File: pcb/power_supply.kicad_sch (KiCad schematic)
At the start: 34 parts

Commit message: Further schematic capture
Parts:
- removed C? (x2): 100u, symbol Device:C_Polarized
- removed C?: 10u, symbol Device:C
- removed U?: AMS1117-3.3, Package_TO_SOT_SMD:SOT-223-3_TabPin2, symbol Regulator_Linear:AMS1117-3.3
- added C?: 100n, symbol Device:C
- added J?: TO_IO, symbol adatv2:Connector_IO
- added U?: 74HC14, symbol 74xx:74HC14
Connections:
- net +3.3V: now also C?.1, J?.5 (3V3), J?.6 (3V3), U?.14 (VCC)
- net +5V: now also J?.3 (5V), J?.4 (5V)
- net GND: now also C?.2, U?.7 (GND)
- new net +12V: J?.1 (12V), J?.2 (12V)
- new net ADAT_IN1: J?.9 (ADAT_IN1)
- new net ADAT_IN2: J?.11 (ADAT_IN2)
- new net ADAT_OUT1: J?.13 (ADAT_OUT1)
- new net ADAT_OUT2: J?.15 (ADAT_OUT2)
- new net ADAT_THRU1: J?.17 (ADAT_THRU1)
- new net ADAT_THRU2: J?.19 (ADAT_THRU2)
- new net GND_IO: J?.10 (GND), J?.12 (GND), J?.14 (GND), J?.16 (GND), J?.18 (GND), J?.20 (GND), J?.7 (GND), J?.8 (GND)
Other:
- moved on the sheet: C?, L?, U?A

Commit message: Further schematic capture
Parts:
- added C? (x4): 100n, symbol Device:C
- added U? (x4): 74LVC2G17, symbol 74xGxx:74LVC2G17
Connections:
- net +3.3V: now also C?.1, C?.1, C?.1, C?.1, U?.5 (VCC), U?.5 (VCC), U?.5 (VCC), U?.5 (VCC)
- net GND: now also C?.2, C?.2, C?.2, C?.2, U?.2 (GND), U?.2 (GND), U?.2 (GND), U?.2 (GND)
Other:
- note added: "FPGA decoupling capacitors"
- note added: "IC supplies"
- note added: "IDC Connector"
- note added: "MCU decoupling capacitors"
- note removed: "FPGA decoupling caps"
- note removed: "MCU decoupling caps"
- moved on the sheet: C?, U?G

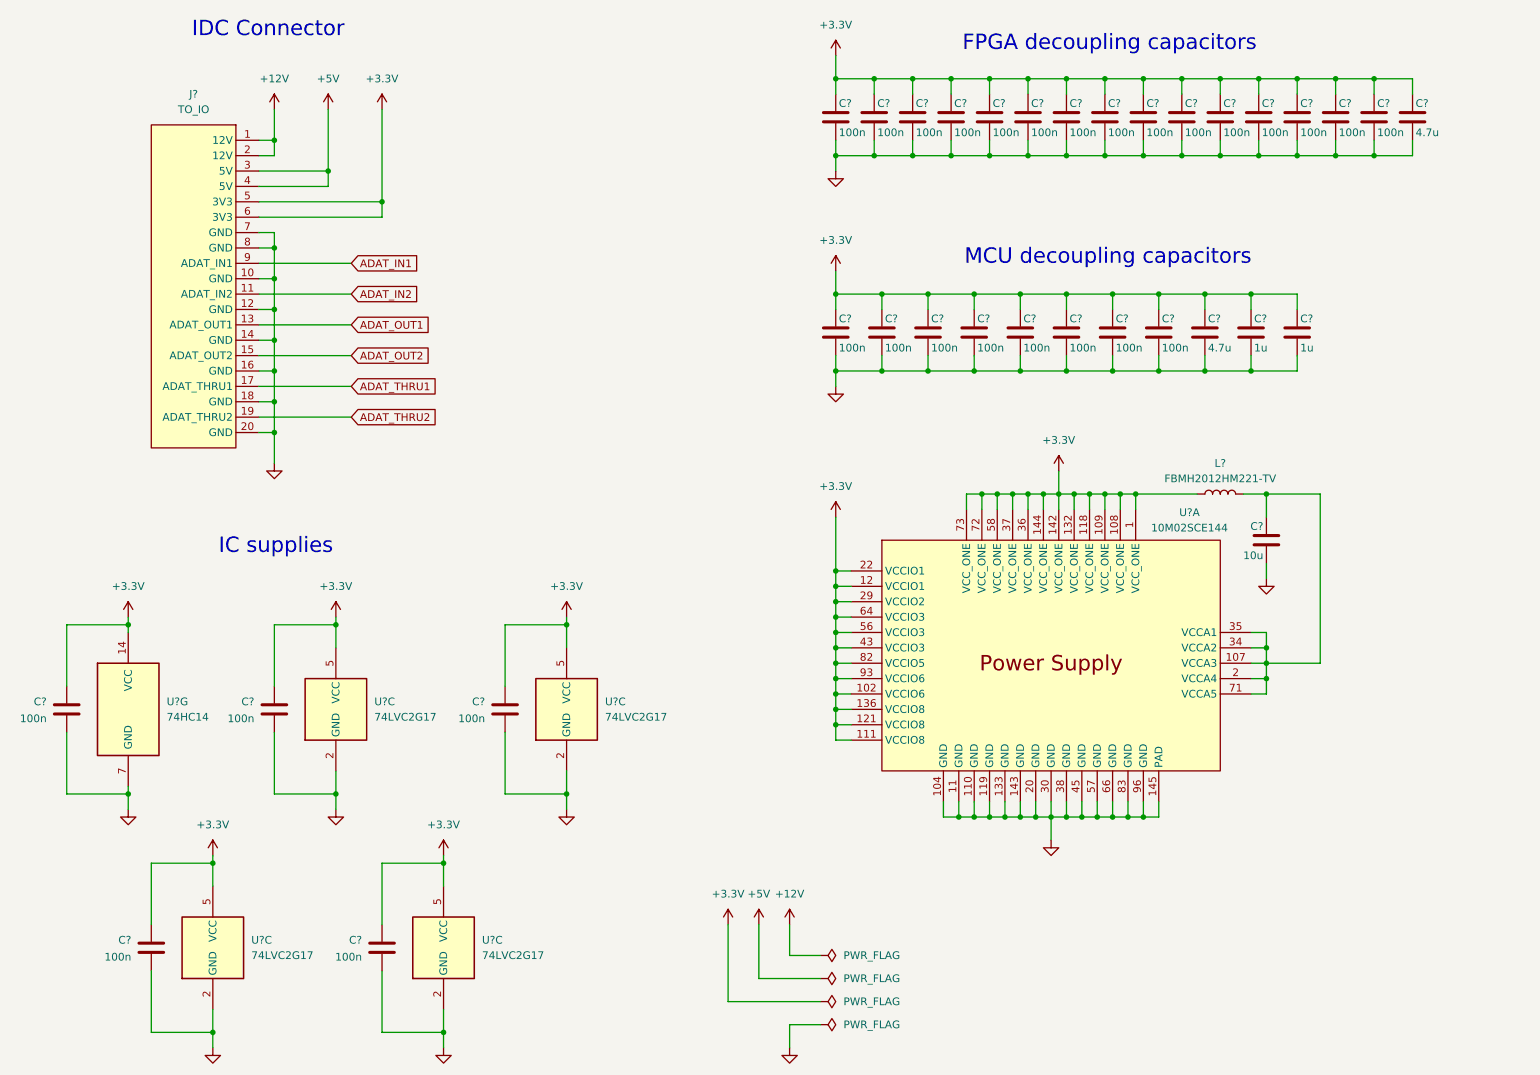
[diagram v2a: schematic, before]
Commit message: Assign most of the footprints to schematic components
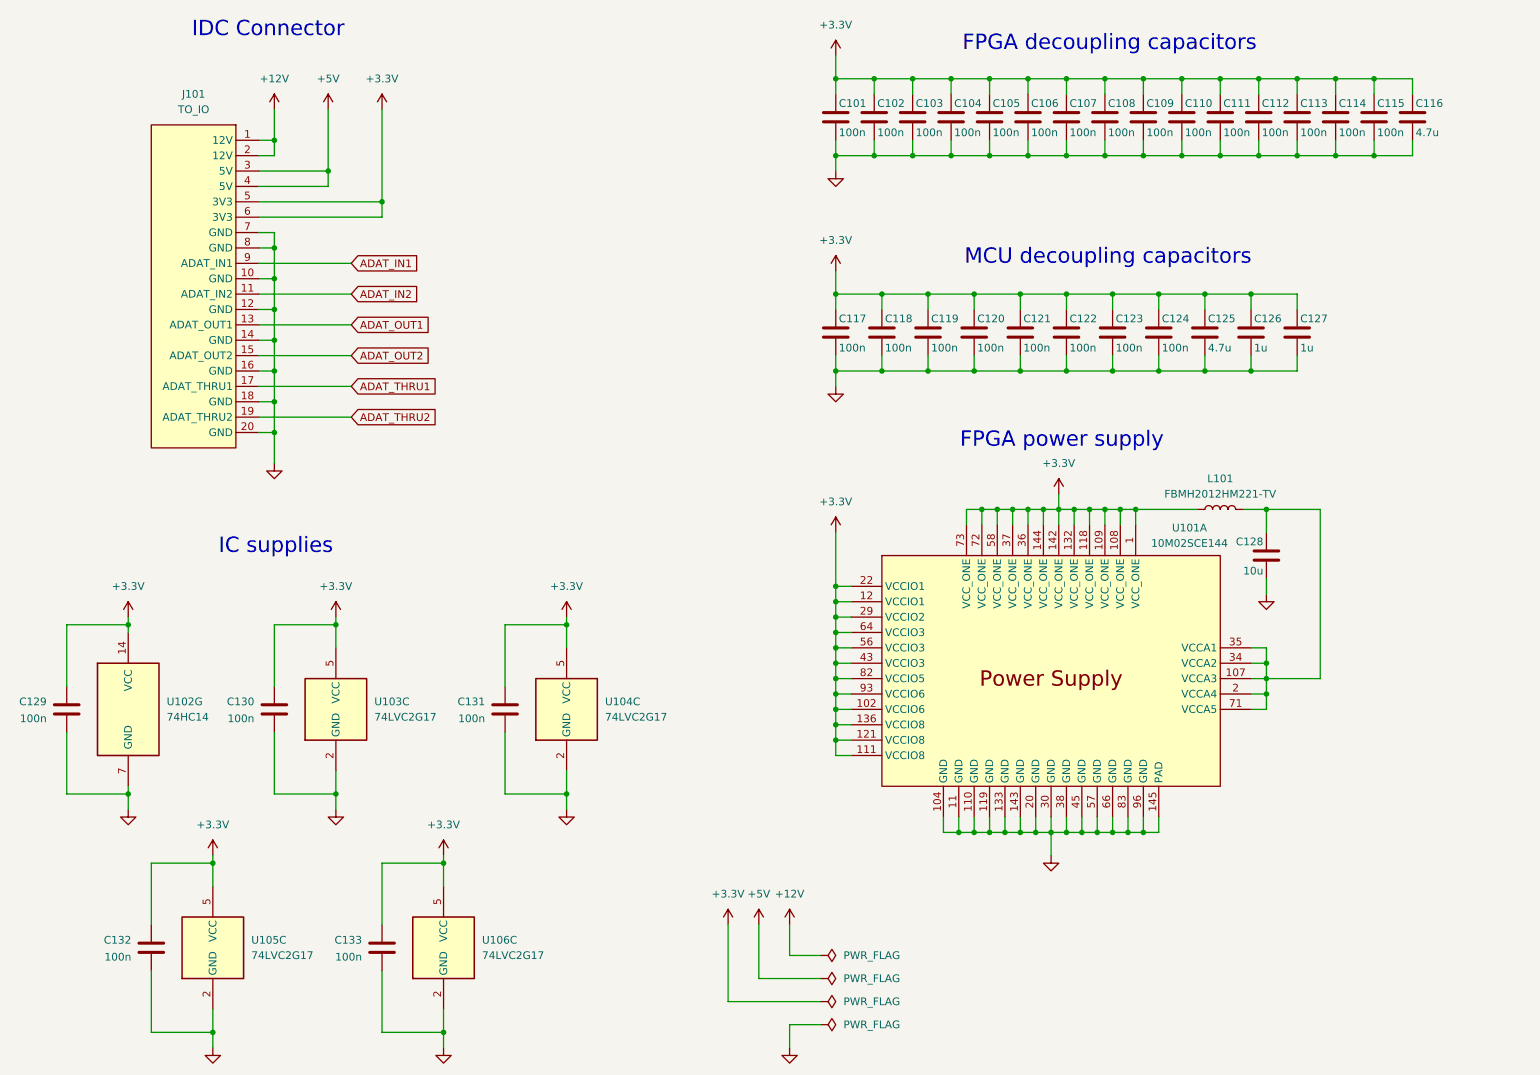
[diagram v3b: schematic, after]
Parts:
- C101, C102, C103, C104, C105, C106, C107, C108, C109, C110, C111, C112, C113, C114, C115, C116, C117, C118, C119, C120, C121, C122, C123, C124, C125, C126, C127, C128, C129, C130, C131, C132, C133: renamed from C?; footprint (none) -> Capacitor_SMD:C_0805_2012Metric_Pad1.18x1.45mm_HandSolder
- J101: renamed from J?; footprint (none) -> Connector_IDC:IDC-Header_2x10_P2.54mm_Vertical
- L101: renamed from L?; footprint (none) -> Inductor_SMD:L_0805_2012Metric_Pad1.15x1.40mm_HandSolder
- gave numbers to parts that had none: 6
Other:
- note added: "FPGA power supply"
- moved on the sheet: C128, L101, U101A

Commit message: Finish assigning footprints to project
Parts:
- U102: footprint (none) -> Package_SO:SOIC-14_3.9x8.7mm_P1.27mm
- U103, U104, U105, U106: footprint (none) -> Package_TO_SOT_SMD:SOT-23-6_Handsoldering
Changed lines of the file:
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@@
 			)
 		)
-		(property "Footprint" ""
+		(property "Footprint" "Package_TO_SOT_SMD:SOT-23-6_Handsoldering"
 			(at 58.42 175.26 0)
 			(effects
@@
 			)
 		)
-		(property "Footprint" ""
+		(property "Footprint" "Package_SO:SOIC-14_3.9x8.7mm_P1.27mm"
 			(at 44.45 135.89 0)
 			(effects
@@
 			)
 		)
-		(property "Footprint" ""
+		(property "Footprint" "Package_TO_SOT_SMD:SOT-23-6_Handsoldering"
 			(at 116.84 135.89 0)
 			(effects
@@
 			)
 		)
-		(property "Footprint" ""
+		(property "Footprint" "Package_TO_SOT_SMD:SOT-23-6_Handsoldering"
 			(at 78.74 135.89 0)
 			(effects
@@
 			)
 		)
-		(property "Footprint" ""
+		(property "Footprint" "Package_TO_SOT_SMD:SOT-23-6_Handsoldering"
 			(at 96.52 175.26 0)
 			(effects

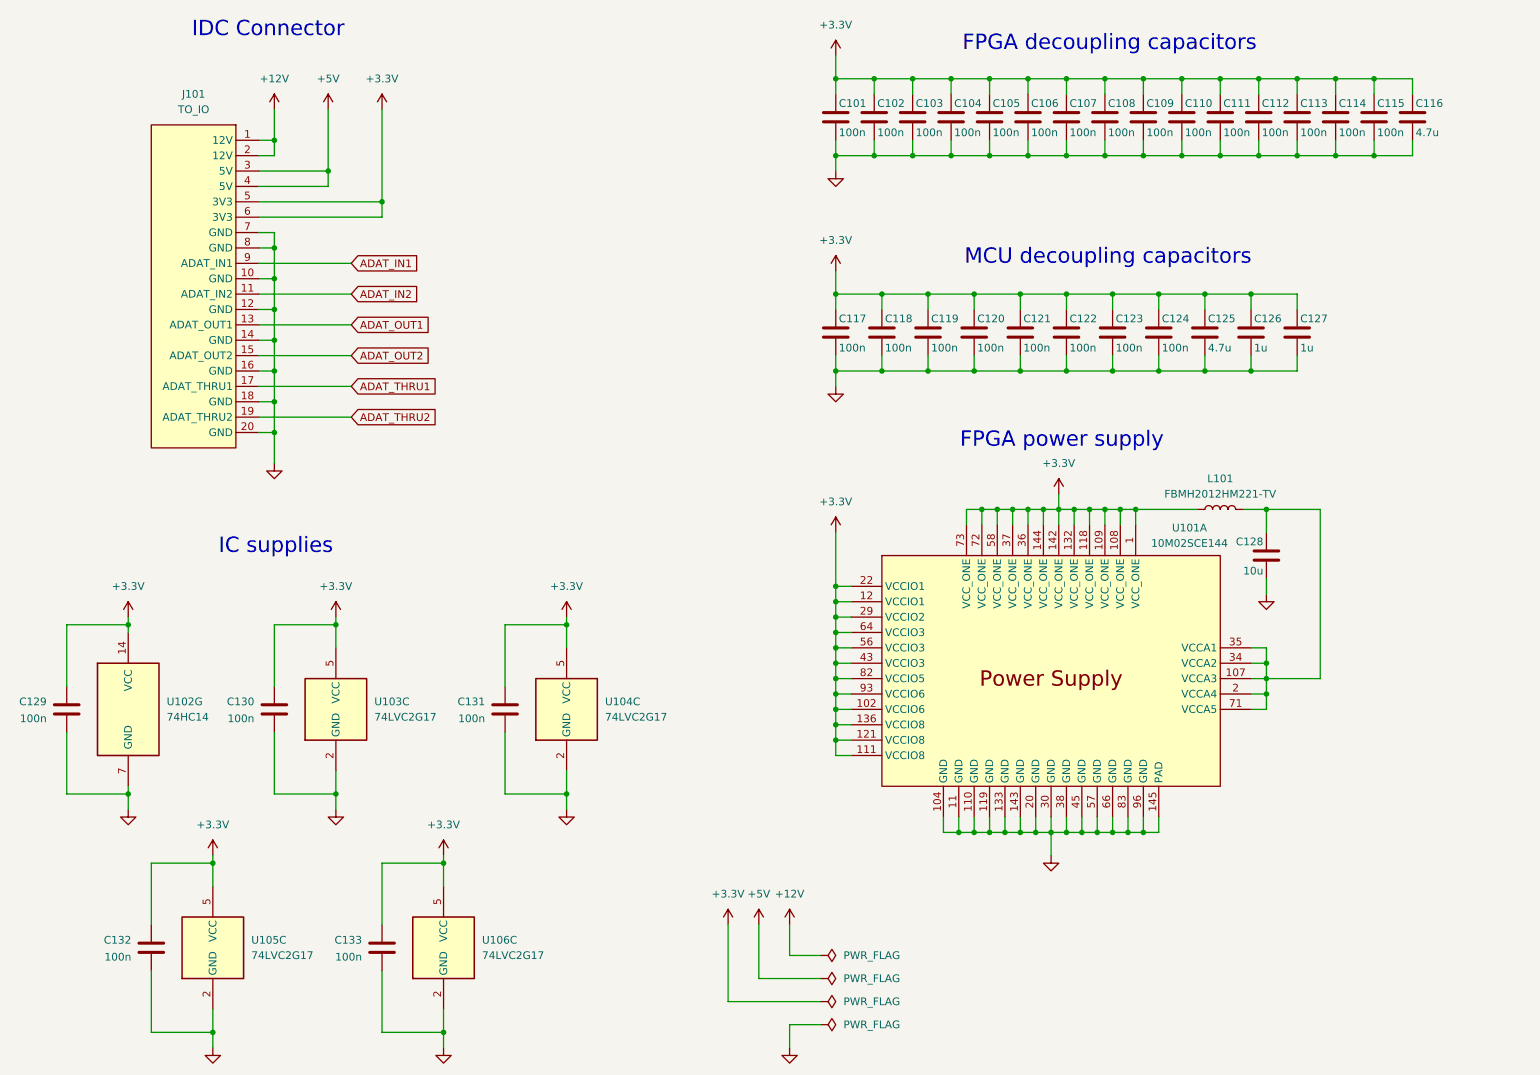
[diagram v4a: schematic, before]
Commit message: Finish drawing IO/Supply board
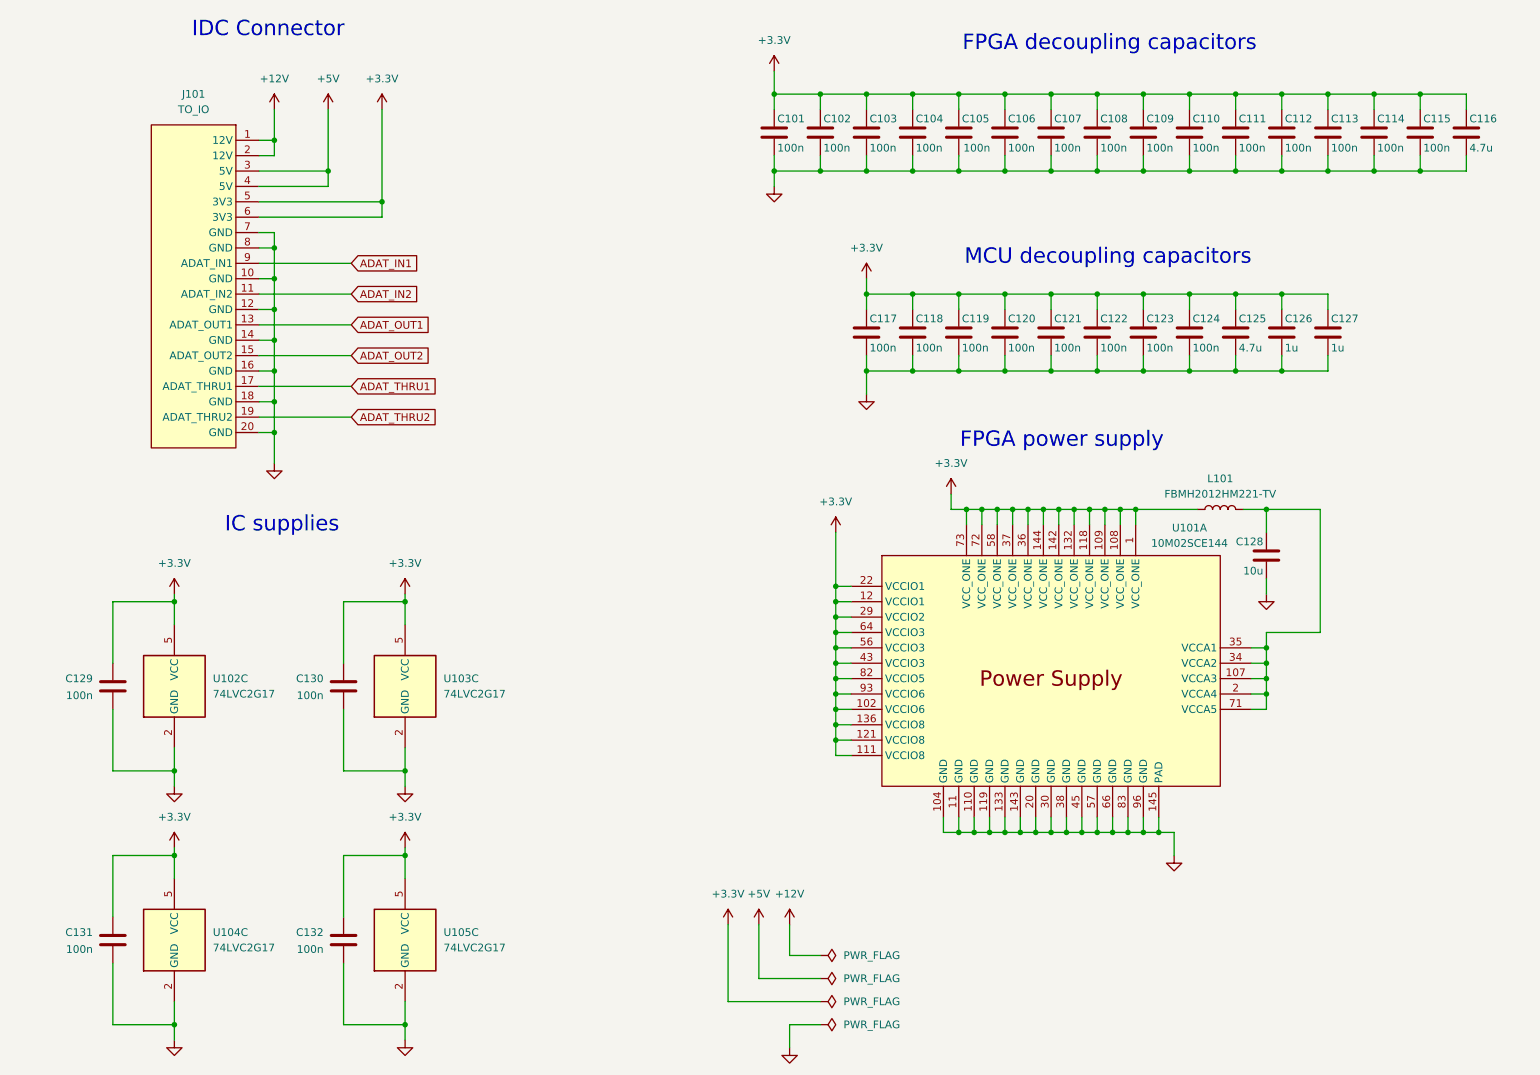
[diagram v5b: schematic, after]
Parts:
- removed C129: 100n, Capacitor_SMD:C_0805_2012Metric_Pad1.18x1.45mm_HandSolder, symbol Device:C
- removed U102: 74HC14, Package_SO:SOIC-14_3.9x8.7mm_P1.27mm, symbol 74xx:74HC14
- C128: footprint Capacitor_SMD:C_0805_2012Metric_Pad1.18x1.45mm_HandSolder -> Capacitor_SMD:C_1206_3216Metric_Pad1.33x1.80mm_HandSolder
- renumbered C130 to C129, C131 to C130, C132 to C131, C133 to C132, U103 to U102, U104 to U103, U105 to U104, U106 to U105
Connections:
- net GND_IO is gone; now on net GND: J101.10 (GND), J101.12 (GND), J101.14 (GND), J101.16 (GND), J101.18 (GND), J101.20 (GND), J101.7 (GND), J101.8 (GND)
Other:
- moved on the sheet: C101, C102, C103, C104, C105, C106, C107, C108, C109, C110, C111, C112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

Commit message: Add missing CAD models of I/O electronic components
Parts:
- U101: footprint Package_QFP:EQFP-144-1EP_20x20mm_P0.5mm_EP4x4mm_ThermalVias -> adatv2:EQFP-144-1EP_20x20mm_P0.5mm_EP4x4mm
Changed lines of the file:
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@@
 			)
 		)
-		(property "Footprint" "Package_QFP:EQFP-144-1EP_20x20mm_P0.5mm_EP4x4mm_ThermalVias"
+		(property "Footprint" "adatv2:EQFP-144-1EP_20x20mm_P0.5mm_EP4x4mm"
 			(at 197.358 79.248 0)
 			(effects
